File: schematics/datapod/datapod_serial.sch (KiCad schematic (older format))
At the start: 10 parts, among them J1 DB9_Female, J2 DB9_Male_MountingHoles, Q3 IRF7324, Q4 FDG1024NZ, U2 MAX232

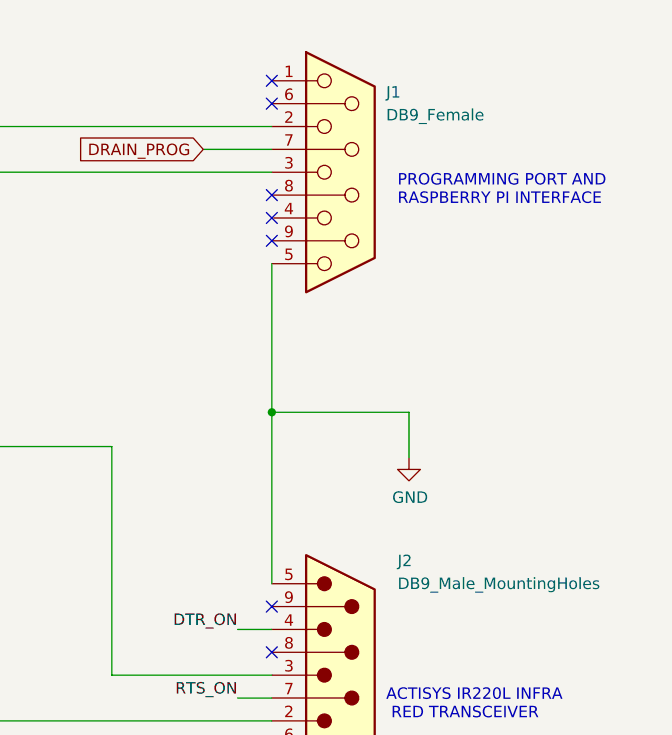
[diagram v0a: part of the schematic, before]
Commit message: added more connectors and started drawing the PCB
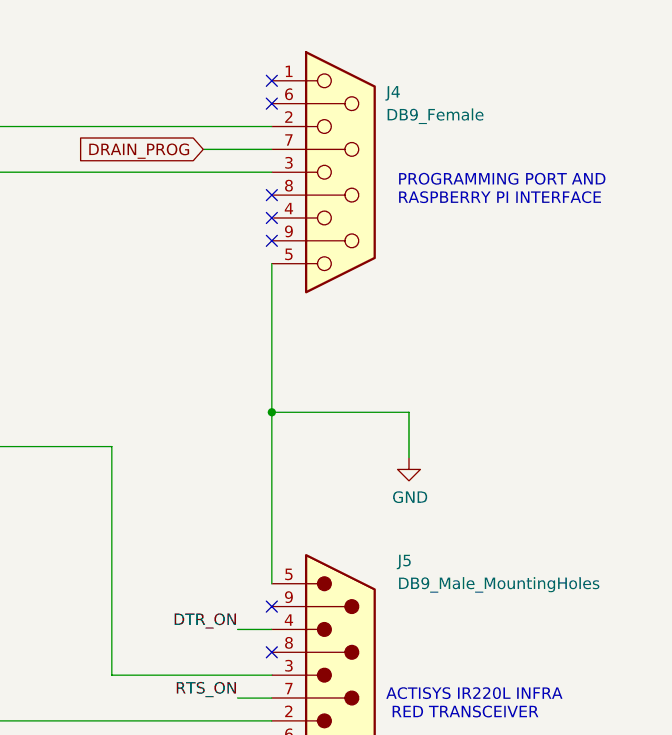
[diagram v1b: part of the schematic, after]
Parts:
- renumbered J1 to J4, J2 to J5
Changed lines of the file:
@@
 P 2900 1400
 AR Path="/5E35C5A7" Ref="#PWR?"  Part="1"
-AR Path="/5E348910/5E35C5A7" Ref="#PWR0118"  Part="1"
-F 0 "#PWR0118" H 2900 1250 50  0001 C CNN
+AR Path="/5E348910/5E35C5A7" Ref="#PWR020"  Part="1"
+F 0 "#PWR020" H 2900 1250 50  0001 C CNN
 F 1 "+5V" H 2915 1573 50  0000 C CNN
 F 2 "" H 2900 1400 50  0001 C CNN
@@
 P 2900 4150
 AR Path="/5E35C5AE" Ref="#PWR?"  Part="1"
-AR Path="/5E348910/5E35C5AE" Ref="#PWR0119"  Part="1"
-F 0 "#PWR0119" H 2900 3900 50  0001 C CNN
+AR Path="/5E348910/5E35C5AE" Ref="#PWR024"  Part="1"
+F 0 "#PWR024" H 2900 3900 50  0001 C CNN
 F 1 "GND" H 2905 3977 50  0000 C CNN
 F 2 "" H 2900 4150 50  0001 C CNN
@@
 P 4200 2650
 AR Path="/5E35C5B9" Ref="#PWR?"  Part="1"
-AR Path="/5E348910/5E35C5B9" Ref="#PWR0120"  Part="1"
-F 0 "#PWR0120" H 4200 2400 50  0001 C CNN
+AR Path="/5E348910/5E35C5B9" Ref="#PWR022"  Part="1"
+F 0 "#PWR022" H 4200 2400 50  0001 C CNN
 F 1 "GND" H 4205 2477 50  0000 C CNN
 F 2 "" H 4200 2650 50  0001 C CNN
@@
 P 4200 2350
 AR Path="/5E35C5C0" Ref="#PWR?"  Part="1"
-AR Path="/5E348910/5E35C5C0" Ref="#PWR0121"  Part="1"
-F 0 "#PWR0121" H 4200 2200 50  0001 C CNN
+AR Path="/5E348910/5E35C5C0" Ref="#PWR021"  Part="1"
+F 0 "#PWR021" H 4200 2200 50  0001 C CNN
 F 1 "+5V" H 4215 2523 50  0000 C CNN
 F 2 "" H 4200 2350 50  0001 C CNN
@@
 P 4850 7600
 AR Path="/5E376729" Ref="#PWR?"  Part="1"
-AR Path="/5E348910/5E376729" Ref="#PWR0122"  Part="1"
-F 0 "#PWR0122" H 4850 7350 50  0001 C CNN
+AR Path="/5E348910/5E376729" Ref="#PWR027"  Part="1"
+F 0 "#PWR027" H 4850 7350 50  0001 C CNN
 F 1 "GND" H 4855 7427 50  0000 C CNN
 F 2 "" H 4850 7600 50  0001 C CNN
@@
 Connection ~ 4750 6450
 $Comp
-L Connector:DB9_Female J1
+L Connector:DB9_Female J4
 U 1 1 5E5A762E
 P 7800 1850
-F 0 "J1" H 8000 2200 50  0000 L CNN
+F 0 "J4" H 8000 2200 50  0000 L CNN
 F 1 "DB9_Female" H 8000 2100 50  0000 L CNN
 F 2 "Connector_Dsub:DSUB-9_Female_Vertical_P2.77x2.84mm_MountingHoles" H 7800 1850 50  0001 C CNN
@@
 P 7800 4950
 AR Path="/5E5B974B" Ref="#PWR?"  Part="1"
-AR Path="/5E348910/5E5B974B" Ref="#PWR0123"  Part="1"
-F 0 "#PWR0123" H 7800 4700 50  0001 C CNN
+AR Path="/5E348910/5E5B974B" Ref="#PWR025"  Part="1"
+F 0 "#PWR025" H 7800 4700 50  0001 C CNN
 F 1 "GND" H 7805 4777 50  0000 C CNN
 F 2 "" H 7800 4950 50  0001 C CNN
@@
 P 8100 3100
 AR Path="/5E5BB053" Ref="#PWR?"  Part="1"
-AR Path="/5E348910/5E5BB053" Ref="#PWR0124"  Part="1"
-F 0 "#PWR0124" H 8100 2850 50  0001 C CNN
+AR Path="/5E348910/5E5BB053" Ref="#PWR023"  Part="1"
+F 0 "#PWR023" H 8100 2850 50  0001 C CNN
 F 1 "GND" H 8105 2927 50  0000 C CNN
 F 2 "" H 8100 3100 50  0001 C CNN
@@
 NoConn ~ 7500 2150
 $Comp
-L Connector:DB9_Male_MountingHoles J2
+L Connector:DB9_Male_MountingHoles J5
 U 1 1 5E6291F0
 P 7800 4050
-F 0 "J2" H 8050 4550 50  0000 L CNN
+F 0 "J5" H 8050 4550 50  0000 L CNN
 F 1 "DB9_Male_MountingHoles" H 8050 4450 50  0000 L CNN
 F 2 "Connector_Dsub:DSUB-9_Male_Vertical_P2.77x2.84mm_MountingHoles" H 7800 4050 50  0001 C CNN
@@
 P 1950 5200
 AR Path="/5E14D46E/5E6C5354" Ref="#PWR?"  Part="1"
-AR Path="/5E348910/5E6C5354" Ref="#PWR0112"  Part="1"
-F 0 "#PWR0112" H 1950 5050 50  0001 C CNN
+AR Path="/5E348910/5E6C5354" Ref="#PWR026"  Part="1"
+F 0 "#PWR026" H 1950 5050 50  0001 C CNN
 F 1 "+5V" H 1965 5373 50  0000 C CNN
 F 2 "" H 1950 5200 50  0001 C CNN

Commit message: added final routed PCB, gerbers and BOM
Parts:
- Q3: Part# (none) -> IRF7324PBFTR-ND; Vendor (none) -> Digikey
- Q4: Part# (none) -> FDG1024NZFSCT-ND; part# FDG1024NZFSCT-ND -> (none)
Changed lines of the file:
@@
 F 3 "http://www.fairchildsemi.com/ds/FD/FDG1024NZ.pdf" H 5050 7350 50  0001 L CNN
 F 4 "Digikey" H 5050 7350 50  0001 C CNN "Vendor"
-F 5 "FDG1024NZFSCT-ND" H 5050 7350 50  0001 C CNN "part#"
+F 5 "FDG1024NZFSCT-ND" H 5050 7350 50  0001 C CNN "Part#"
 	2    5050 7350
 	-1   0    0    -1
@@
 F 3 "http://www.fairchildsemi.com/ds/FD/FDG1024NZ.pdf" H 4650 7350 50  0001 L CNN
 F 4 "Digikey" H 4650 7350 50  0001 C CNN "Vendor"
-F 5 "FDG1024NZFSCT-ND" H 4650 7350 50  0001 C CNN "part#"
+F 5 "FDG1024NZFSCT-ND" H 4650 7350 50  0001 C CNN "Part#"
 	1    4650 7350
 	1    0    0    -1
@@
 F 2 "Package_SO:SOIC-8_3.9x4.9mm_P1.27mm" H 1950 5575 50  0001 L CNN
 F 3 "http://www.infineon.com/dgdl/irf7324pbf.pdf?fileId=5546d462533600a4015355f5f0861b4b" H 1750 5650 50  0001 L CNN
+F 4 "Digikey" H 1750 5650 50  0001 C CNN "Vendor"
+F 5 "IRF7324PBFTR-ND" H 1750 5650 50  0001 C CNN "Part#"
 	1    1750 5650
 	1    0    0    1
@@
 F 2 "Package_SO:SOIC-8_3.9x4.9mm_P1.27mm" H 2350 5575 50  0001 L CNN
 F 3 "http://www.infineon.com/dgdl/irf7324pbf.pdf?fileId=5546d462533600a4015355f5f0861b4b" H 2150 5650 50  0001 L CNN
+F 4 "Digikey" H 2150 5650 50  0001 C CNN "Vendor"
+F 5 "IRF7324PBFTR-ND" H 2150 5650 50  0001 C CNN "Part#"
 	2    2150 5650
 	-1   0    0    1

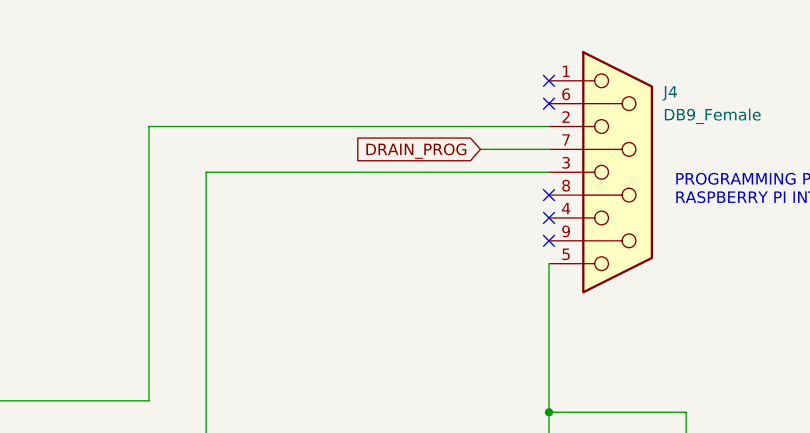
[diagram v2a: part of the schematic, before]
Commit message: replaced rn2 with 4 resistors and moved sd card closer to mcu
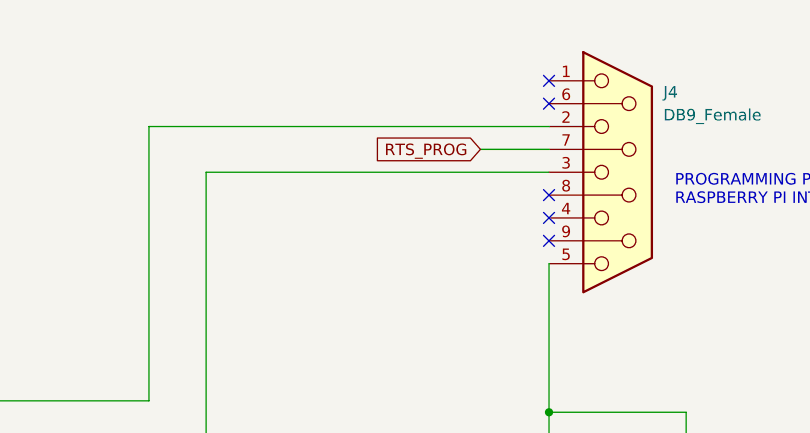
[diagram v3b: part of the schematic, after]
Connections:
- net DRAIN_PROG: no longer J4.7
- net RTS_PROG: now also J4.7
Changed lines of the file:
@@
 EESchema Schematic File Version 4
-LIBS:datapod-cache
+LIBS:_autosave-datapod-cache
 EELAYER 30 0
 EELAYER END
@@
 	6000 1850 7500 1850
 Text GLabel 7200 1750 0    50   Input ~ 0
-DRAIN_PROG
+RTS_PROG
 Wire Wire Line
 	7200 1750 7500 1750

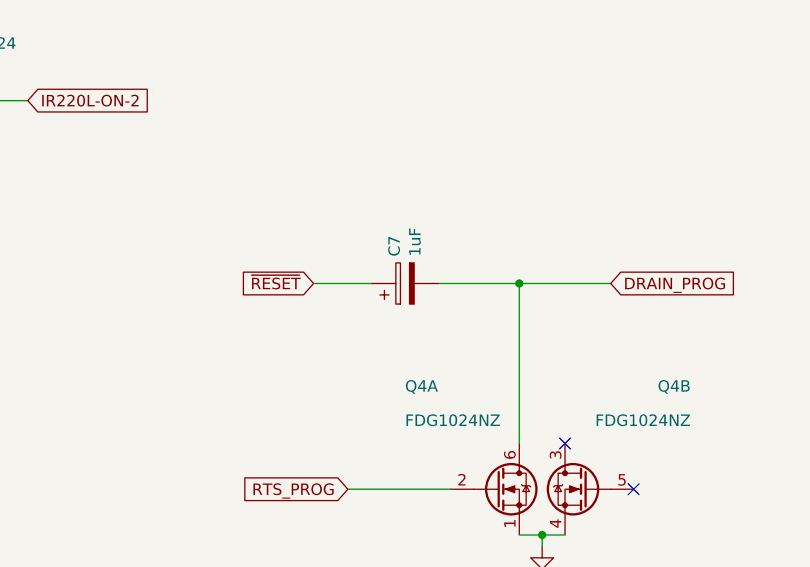
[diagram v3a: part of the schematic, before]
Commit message: added 3d models that somehow were lost.
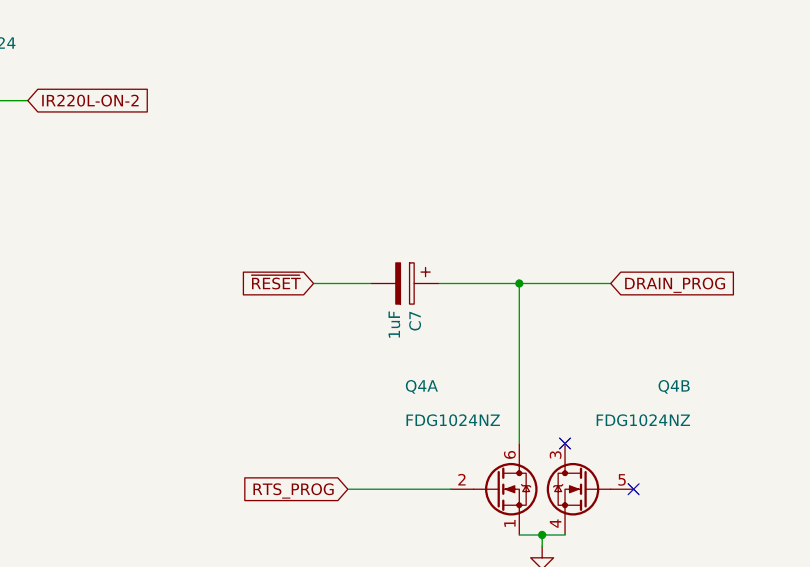
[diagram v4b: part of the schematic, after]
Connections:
- net DRAIN_PROG: now also C7.1; no longer C7.2
- net ~RESET: now also C7.2; no longer C7.1
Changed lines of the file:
@@
 F 5 " TCJP105M025R0500" H 4250 6450 50  0001 C CNN "Part#"
 	1    4250 6450
-	0    -1   -1   0
+	0    1    1    0
 $EndComp
 Text GLabel 3850 6450 0    50   Input ~ 0

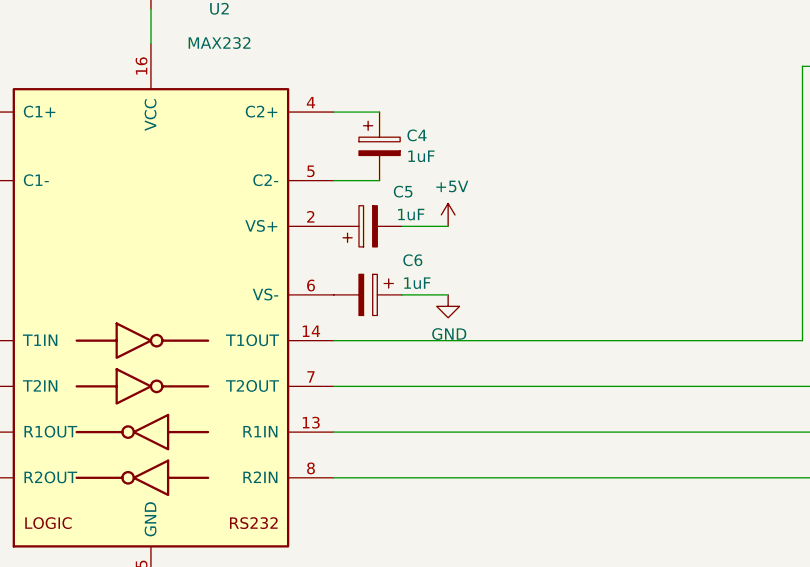
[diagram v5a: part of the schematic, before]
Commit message: fixed bad gnd trace on 3.3v circuit and added comments to the silkscreen
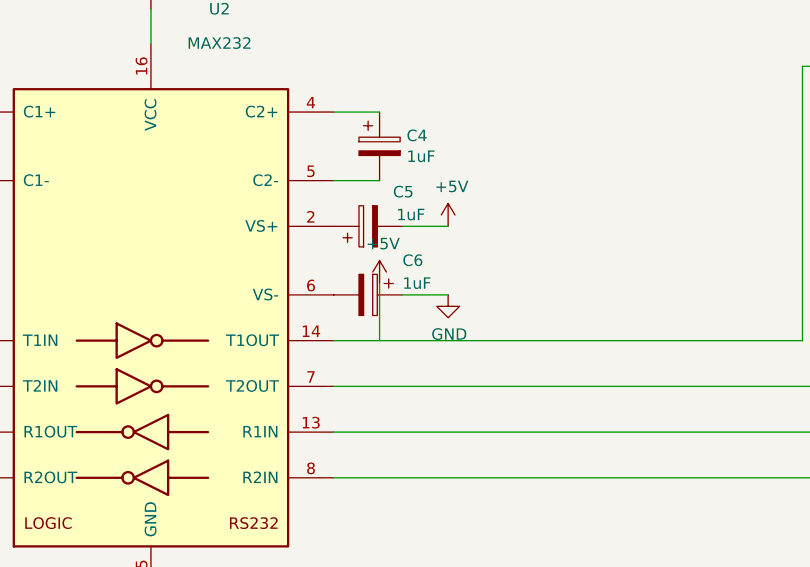
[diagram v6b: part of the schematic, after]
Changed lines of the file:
@@
 $EndComp
-Wire Wire Line
-	2900 3950 2900 4150
 Wire Wire Line
 	2100 1850 1950 1850
@@
 	1    0    0    -1
 $EndComp
-Wire Wire Line
-	4000 2350 4200 2350
 Text GLabel 2100 2850 0    50   Input ~ 0
 MCU-TX
@@
 Wire Wire Line
 	4450 7350 4000 7350
+Wire Wire Line
+	4200 2350 4000 2350
+Wire Wire Line
+	2900 3950 2900 4150
+$Comp
+L power:+5V #PWR?
+U 1 1 5E291178
+P 3900 2600
+F 0 "#PWR?" H 3900 2450 50  0001 C CNN
+F 1 "+5V" H 3915 2773 50  0000 C CNN
+F 2 "" H 3900 2600 50  0001 C CNN
+F 3 "" H 3900 2600 50  0001 C CNN
+	1    3900 2600
+	1    0    0    -1
+$EndComp
+Wire Wire Line
+	3900 2850 3900 2600
 $EndSCHEMATC

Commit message: added rtc stuff , rotated db9s , added on/off transistors for max chip and sdcard
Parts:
- added JP2: SolderJumper_3_Open, Jumper:SolderJumper-3_P1.3mm_Open_RoundedPad1.0x1.5mm, symbol Jumper:SolderJumper_3_Open
- J4: footprint Connector_Dsub:DSUB-9_Female_Vertical_P2.77x2.84mm_MountingHoles -> Connector_Dsub:DSUB-9_Female_Horizontal_P2.77x2.84mm_EdgePinOffset7.70mm_Housed_MountingHolesOffset9.12mm; Part# 609-5190-ND -> AE10921-ND
- J5: footprint Connector_Dsub:DSUB-9_Male_Vertical_P2.77x2.84mm_MountingHoles -> Connector_Dsub:DSUB-9_Male_Horizontal_P2.77x2.84mm_EdgePinOffset7.70mm_Housed_MountingHolesOffset9.12mm; Part# 609-5184-ND -> AE10968-ND
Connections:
- net GND: now also JP2.1 (A); no longer U2.15 (GND)
- net at Q4.3 (D): now also JP2.3 (B)
- net RS232_DRIVER_ON_OFF: now reaches Q4.5 (G)
- new net: JP2.2 (C), U2.15 (GND)
- no-connect marks 11 -> 9
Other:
- note added: "Solder this jumper to ground for programming\nthrough the serial port. Solder this jumper to\nthe other side to power the max chip via the\nmosfet. This is to save power."
